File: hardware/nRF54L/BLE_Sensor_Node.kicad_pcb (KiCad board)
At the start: 4 copper layers, 34 x 34 mm, 42 parts, among them U1 nRF54L05-QFXX, U2 SHTC3, U3 HDC2010, X1 32MHz, X2 32.768kHz

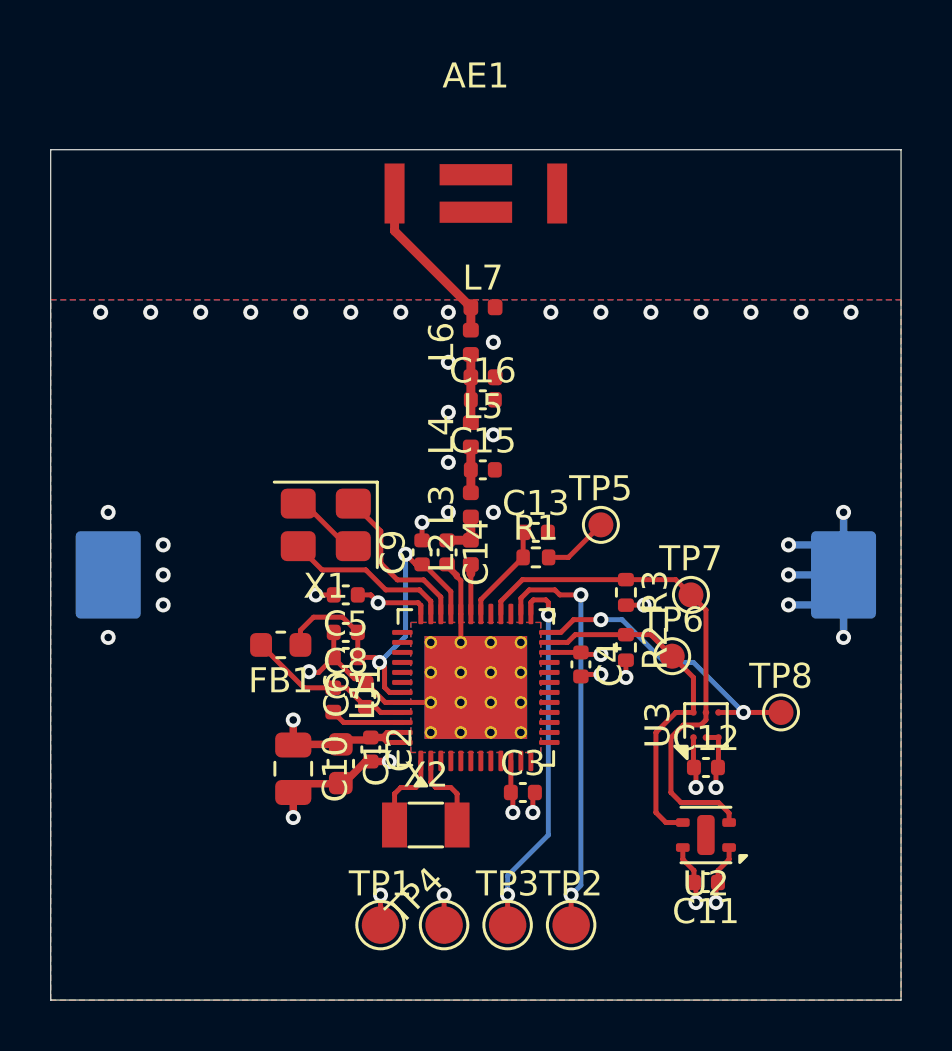
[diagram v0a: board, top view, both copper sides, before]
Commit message: Added optional U.FL connector and stiching vias
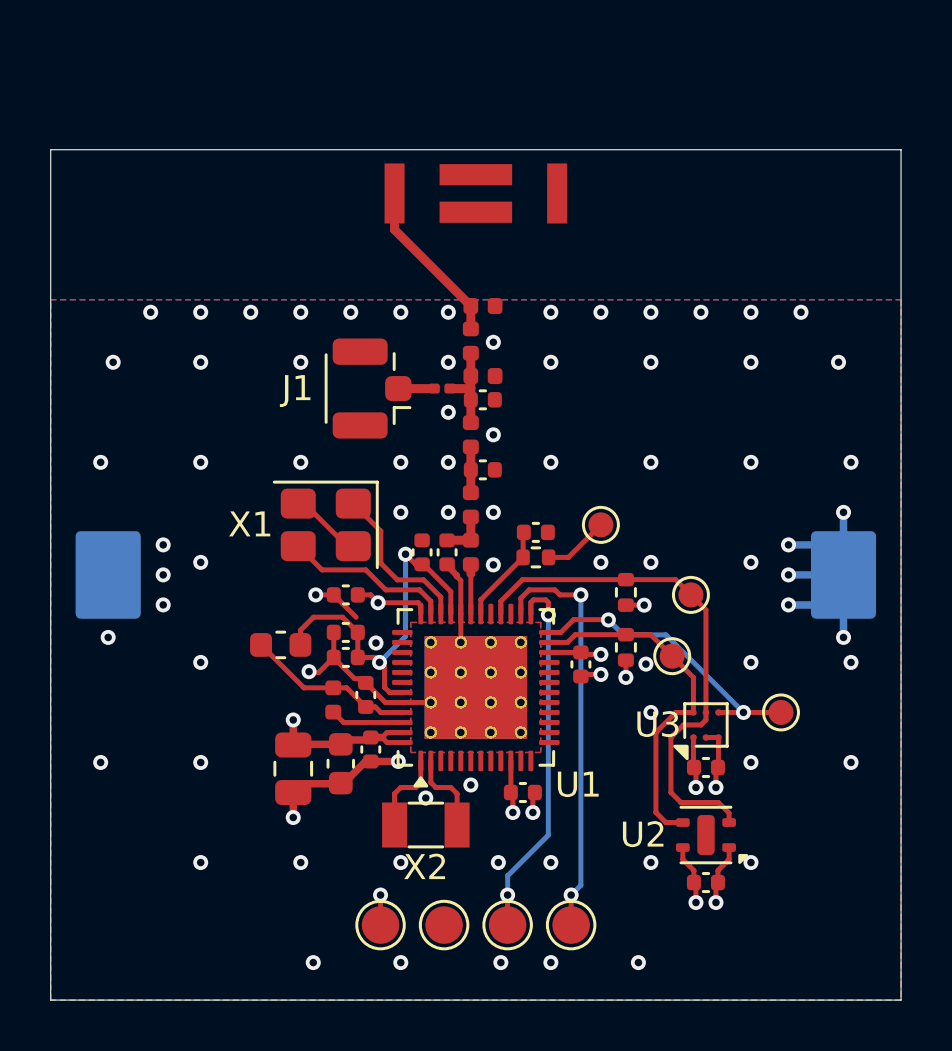
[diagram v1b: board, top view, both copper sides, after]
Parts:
- added J1: Conn_Coaxial_Small, Connector_Coaxial:U.FL_Hirose_U.FL-R-SMT-1_Vertical, F.Cu at (145.4, 92.5)
- added R4: R, Resistor_SMD:R_0201_0603Metric, F.Cu at (148.7, 92.5)
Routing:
- net Net-(J1-In): track 0.00 -> 1.43 mm
- net Net-(C16-Pad1): track 2.73 -> 3.61 mm
- net GND: track 27.8 -> 27.5 mm, vias 37 -> 77

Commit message: First Rev of the nRF variant
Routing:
- net GND: track 27.5 -> 28.1 mm, vias 77 -> 78
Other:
- board text added: "+"
- board text added: "-"
- board text added: "BSN-N54-A"
- board text added: "C"
- board text added: "D"
- board text added: "RST"
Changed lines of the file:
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@@
 		(capping no)
 		(filling no)
-		(zone_defaults)
 		(pcbplotparams
 			(layerselection 0x00000000_00000000_55555555_5755f5ff)
@@
 		(layer "Edge.Cuts")
 	)
+	(gr_text "+"
+		(at 146.19 115.6 0)
+		(layer "F.SilkS")
+		(effects
+			(font
+				(size 1 1)
+				(thickness 0.15)
+			)
+		)
+	)
+	(gr_text "-"
+		(at 148.73 115.6 0)
+		(layer "F.SilkS")
+		(effects
+			(font
+				(size 1 1)
+				(thickness 0.15)
+			)
+		)
+	)
+	(gr_text "D"
+		(at 151.3 115.9 0)
+		(layer "F.SilkS")
+		(effects
+			(font
+				(size 1 1)
+				(thickness 0.15)
+			)
+		)
+	)
+	(gr_text "C"
+		(at 153.8 115.9 0)
+		(layer "F.SilkS")
+		(effects
+			(font
+				(size 1 1)
+				(thickness 0.15)
+			)
+		)
+	)
+	(gr_text "RST"
+		(at 157.2 98 0)
+		(layer "F.SilkS")
+		(effects
+			(font
+				(size 1 1)
+				(thickness 0.15)
+			)
+		)
+	)
+	(gr_text "RST"
+		(at 160.1 103.4 0)
+		(layer "F.SilkS")
+		(effects
+			(font
+				(size 1 1)
+				(thickness 0.15)
+			)
+		)
+	)
+	(gr_text "RST"
+		(at 160.8 100.8 0)
+		(layer "F.SilkS")
+		(effects
+			(font
+				(size 1 1)
+				(thickness 0.15)
+			)
+		)
+	)
+	(gr_text "RST"
+		(at 164.5 105.5 0)
+		(layer "F.SilkS")
+		(effects
+			(font
+				(size 1 1)
+				(thickness 0.15)
+			)
+		)
+	)
+	(gr_text "BSN-N54-A"
+		(at 150 114 0)
+		(layer "B.SilkS")
+		(effects
+			(font
+				(size 1.5 1.5)
+				(thickness 0.2)
+			)
+			(justify mirror)
+		)
+	)
 	(segment
 		(start 146.25 106.5)
@@
 	)
 	(segment
+		(start 151.4 95.8)
+		(end 150.76 95.8)
+		(width 0.3)
+		(layer "F.Cu")
+		(net "GND")
+	)
+	(segment
 		(start 149.4 101.5625)
 		(end 149.4 102.7)
@@
 	)
 	(via
+		(at 151.4 95.8)
+		(size 0.6)
+		(drill 0.3)
+		(layers "F.Cu" "B.Cu")
+		(net "GND")
+	)
+	(via
 		(at 155 89.5)
 		(size 0.6)
@@
 	)
 	(segment
+		(start 149.8 91.135)
+		(end 149.8 92.55)
+		(width 0.3586)
+		(layer "F.Cu")
+		(net "Net-(C16-Pad1)")
+	)
+	(segment
+		(start 149.8 92.55)
+		(end 149.8 93.915)
+		(width 0.3586)
+		(layer "F.Cu")
+		(net "Net-(C16-Pad1)")
+	)
+	(segment
+		(start 148.97 92.55)
+		(end 149.8 92.55)
+		(width 0.3586)
+		(layer "F.Cu")
+		(net "Net-(C16-Pad1)")
+	)
+	(segment
+		(start 146.9 92.55)
+		(end 148.33 92.55)
+		(width 0.3586)
+		(layer "F.Cu")
+		(net "Net-(J1-In)")
+	)
+	(segment
 		(start 151.890001 99.3)
 		(end 151.890001 98.329999)
@@
 		(net "Net-(U1-DCC)")
 	)
-	(segment
-		(start 146.9 92.55)
-		(end 148.33 92.55)
-		(width 0.3586)
-		(layer "F.Cu")
-		(net "Net-(J1-In)")
-	)
-	(segment
-		(start 149.8 91.135)
-		(end 149.8 92.55)
-		(width 0.3586)
-		(layer "F.Cu")
-		(net "Net-(C16-Pad1)")
-	)
-	(segment
-		(start 149.8 92.55)
-		(end 149.8 93.915)
-		(width 0.3586)
-		(layer "F.Cu")
-		(net "Net-(C16-Pad1)")
-	)
-	(segment
-		(start 148.97 92.55)
-		(end 149.8 92.55)
-		(width 0.3586)
-		(layer "F.Cu")
-		(net "Net-(C16-Pad1)")
-	)
 	(zone
 		(layer "F.Cu")
@@
 		(polygon
 			(pts
+				(xy 152.5 98.5) (xy 154.5 98.5) (xy 154.5 100) (xy 152.5 100)
+			)
+		)
+	)
+	(zone
+		(layer "F.Cu")
+		(hatch edge 0.5)
+		(connect_pads
+			(clearance 0)
+		)
+		(min_thickness 0.15)
+		(keepout
+			(tracks allowed)
+			(vias allowed)
+			(pads allowed)
+			(copperpour not_allowed)
+			(footprints allowed)
+		)
+		(placement
+			(enabled no)
+			(sheetname "/")
+		)
+		(fill
+			(thermal_gap 0.5)
+			(thermal_bridge_width 0.3)
+			(island_removal_mode 0)
+		)
+		(polygon
+			(pts
 				(xy 144.103148 101) (xy 144.506133 100.994031) (xy 144.506133 101.2) (xy 144.103148 101.2)
 			)
@@
 			(thermal_gap 0.5)
 			(thermal_bridge_width 0.3)
-			(smoothing fillet)
-			(radius 0.5)
 			(island_removal_mode 0)
 		)
@@
 			)
 		)
+	)
+	(zone
+		(layers "F.Cu" "In1.Cu" "In2.Cu")
+		(hatch edge 0.5)
+		(connect_pads
+			(clearance 0)
+		)
+		(min_thickness 0.15)
+		(keepout
+			(tracks allowed)
+			(vias allowed)
+			(pads allowed)
+			(copperpour not_allowed)
+			(footprints allowed)
+		)
+		(placement
+			(enabled no)
+			(sheetname "/")
+		)
+		(fill
+			(thermal_gap 0.5)
+			(thermal_bridge_width 0.3)
+			(island_removal_mode 0)
+		)
+		(polygon
+			(pts
+				(xy 150.4 95) (xy 151.2 95) (xy 151.7 95.2) (xy 151.9 95.6) (xy 151.9 96) (xy 151.7 96.4) (xy 151.2 96.6)
+				(xy 150.4 96.6)
+			)
+		)
